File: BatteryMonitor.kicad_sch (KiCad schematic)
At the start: 17 parts, among them U3 MAX17205G+

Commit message: First pass at new schematics and board
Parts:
- added NT1: NetTie_2, NetTie:NetTie-2_SMD_Pad2.0mm, symbol Device:NetTie_2
- C5, C6, C7, C8, C9, TH1, TH2, TH3, TH4, TH5, TH6: footprint (none) -> Capacitor_SMD:C_0603_1608Metric
- R10, R11: value 10k -> 30k; footprint (none) -> Resistor_SMD:R_0603_1608Metric
- R3, R8: footprint (none) -> Resistor_SMD:R_0603_1608Metric
- R9: footprint (none) -> Resistor_SMD:R_2512_6332Metric
- U3: footprint 21-0137_T1433+2C_MXM -> Battery-Board:21-0137_T1433&plus_2C_MXM
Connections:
- net SYSTEM_VSS: now also NT1.2; no longer C7.2, C8.2, C9.2, R9.1, U3.15 (EP), U3.4 (CSN)
- new net CSN: C7.2, C8.2, C9.2, NT1.1, R9.1, U3.15 (EP), U3.4 (CSN)

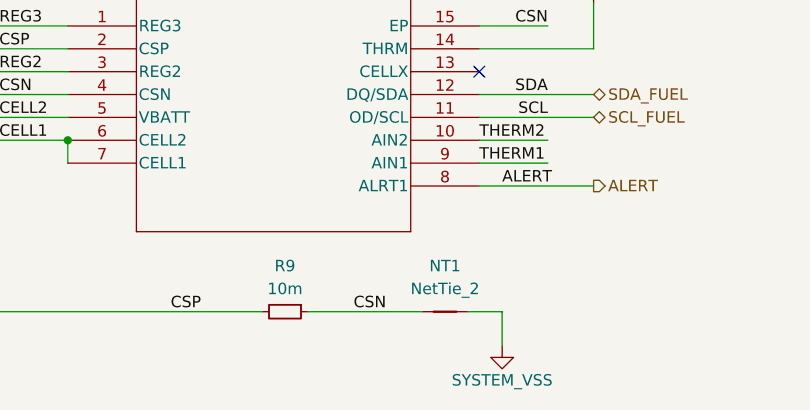
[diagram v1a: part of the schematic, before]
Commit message: Updated footprint to follow PC/104
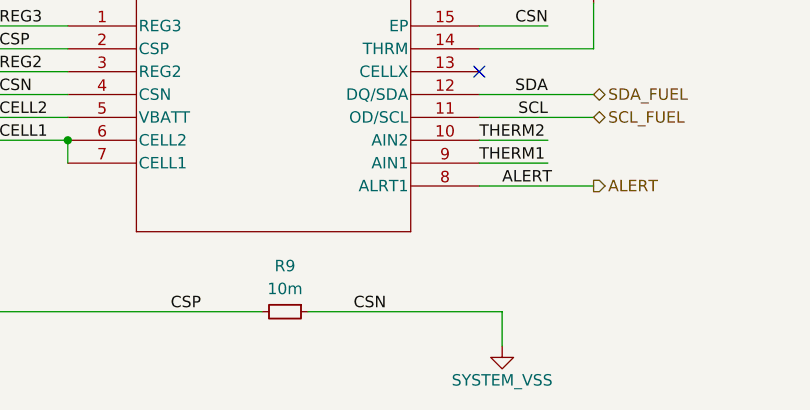
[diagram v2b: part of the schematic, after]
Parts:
- removed NT1: NetTie_2, NetTie:NetTie-2_SMD_Pad2.0mm, symbol Device:NetTie_2
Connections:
- net CSN is gone; now on net SYSTEM_VSS: C7.2, C8.2, C9.2, R9.1, U3.15 (EP), U3.4 (CSN)
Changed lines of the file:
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@@
-	(wire
-		(pts
-			(xy 143.51 137.16) (xy 147.32 137.16)
-		)
-		(stroke
-			(width 0)
-			(type default)
-		)
-	)
 	(wire
 		(pts
@@
 	(wire
 		(pts
-			(xy 125.73 137.16) (xy 138.43 137.16)
+			(xy 125.73 137.16) (xy 147.32 137.16)
 		)
 		(stroke
@@
 					(unit 1)
 				)
-			)
-		)
-	)
-	(symbol
-		(lib_id "Device:NetTie_2")
-		(at 140.97 137.16 0)
-		(unit 1)
-		(exclude_from_sim no)
-		(in_bom no)
-		(on_board yes)
-		(dnp no)
-		(fields_autoplaced yes)
-		(property "Reference" "NT1"
-			(at 140.97 132.08 0)
-			(effects
-				(font
-					(size 1.27 1.27)
-				)
-			)
-		)
-		(property "Value" "NetTie_2"
-			(at 140.97 134.62 0)
-			(effects
-				(font
-					(size 1.27 1.27)
-				)
-			)
-		)
-		(property "Footprint" "NetTie:NetTie-2_SMD_Pad2.0mm"
-			(at 140.97 137.16 0)
-			(effects
-				(font
-					(size 1.27 1.27)
-				)
-				(hide yes)
-			)
-		)
-		(property "Datasheet" "~"
-			(at 140.97 137.16 0)
-			(effects
-				(font
-					(size 1.27 1.27)
-				)
-				(hide yes)
-			)
-		)
-		(property "Description" "Net tie, 2 pins"
-			(at 140.97 137.16 0)
-			(effects
-				(font
-					(size 1.27 1.27)
-				)
-				(hide yes)
-			)
-		)
-		(pin "2"
-		)
-		(pin "1"
-		)
-		(instances
-			(project "BatteryBoard"
-				(path "/b6fd875d-6e05-4440-9a05-0f0aa046a0ef/ad142cc2-d77f-4a6c-99c2-d9e17f4c27ae"
-					(reference "NT1")
-					(unit 1)
-				)
